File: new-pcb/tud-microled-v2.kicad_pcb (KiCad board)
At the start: 2 copper layers, 100 x 80 mm, 153 parts

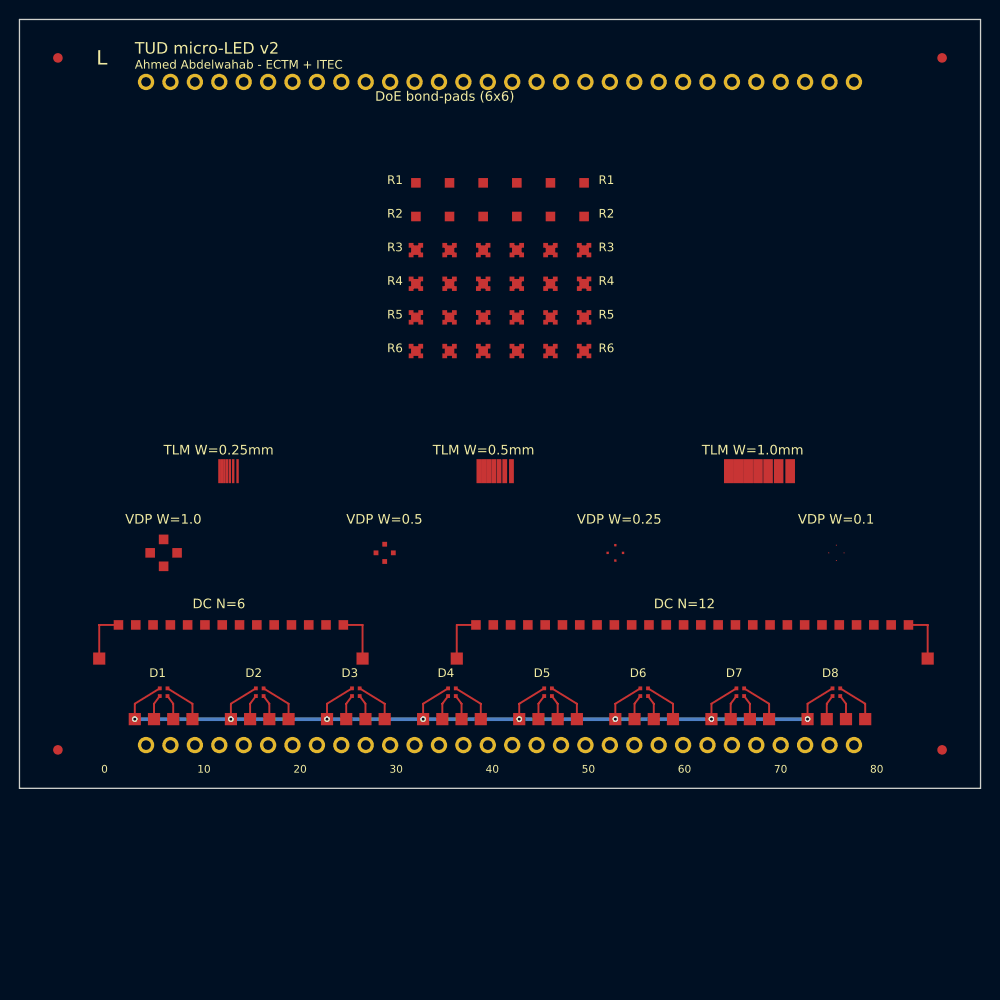
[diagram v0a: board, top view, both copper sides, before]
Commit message: Refactor PCB design settings and update electrical test configuration
- Added a new user-edited backup file for the PCB design with comprehensive settings for design defaults, rules, and dimensions.
- Updated the electrical test configuration by modifying the column widths to ensure proper alignment and sorting in the report.
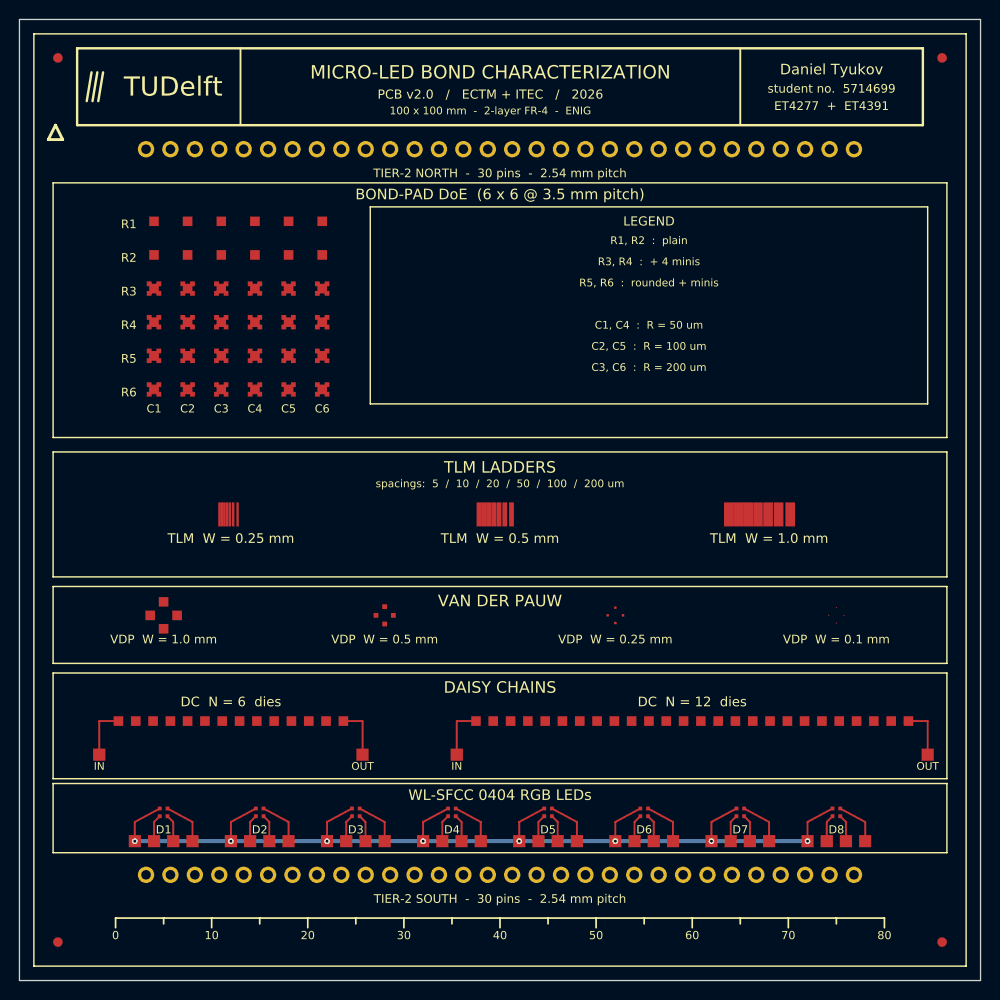
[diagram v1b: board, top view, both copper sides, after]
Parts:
- moved BP_R1C1 27.5 mm to (14.0, 21.0)
- moved BP_R1C2 27.5 mm to (17.5, 21.0)
- moved BP_R1C3 27.5 mm to (21.0, 21.0)
- moved BP_R1C4 27.5 mm to (24.5, 21.0)
- moved BP_R1C5 27.5 mm to (28.0, 21.0)
- moved BP_R1C6 27.5 mm to (31.5, 21.0)
- moved BP_R2C1 27.5 mm to (14.0, 24.5)
- moved BP_R2C2 27.5 mm to (17.5, 24.5)
- moved BP_R2C3 27.5 mm to (21.0, 24.5)
- moved BP_R2C4 27.5 mm to (24.5, 24.5)
- moved BP_R2C5 27.5 mm to (28.0, 24.5)
- moved BP_R2C6 27.5 mm to (31.5, 24.5)
- moved BP_R3C1 27.5 mm to (14.0, 28.0)
- moved BP_R3C2 27.5 mm to (17.5, 28.0)
- moved BP_R3C3 27.5 mm to (21.0, 28.0)
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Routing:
- net LED_VCC: track 107.2 -> 109.6 mm
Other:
- board size 100 x 80 mm -> 100 x 100 mm
- board text added: "100 x 100 mm - 2-layer FR-4 - ENIG"
- board text added: "2-layer FR-4 1.6 mm 1 oz Cu"
- board text added: "ASSEMBLY"
- board text added: "BOND-PAD DoE (6 x 6 @ 3.5 mm pitch)"
- board text added: "BOTTOM - tud-microled-v2 - 2026"
- board text added: "Bonder: Tresky T-3000-PRO"
- board text added: "C1"
- board text added: "C1, C4 : R = 50 um"
- board text added: "C2"
- board text added: "C2, C5 : R = 100 um"
- board text added: "C3"
- board text added: "C3, C6 : R = 200 um"
- board text added: "C4"
- board text added: "C5"
- board text added: "C6"
- board text added: "D1..D8 + PP-* - LEDs and probes"
- board text added: "DAISY CHAINS"
- board text added: "DC - daisy chain (N joints)"
- board text added: "DC N = 12 dies"
- board text added: "DC N = 6 dies"
- board text added: "DESIGNER"
- board text added: "Daniel Tyukov"
- board text added: "Daniel Tyukov - student no. 5714699"
- board text added: "DoE - 6 x 6 isolated bond pads"
- board text added: "ET4277 + ET4391"
- board text added: "ET4277 + ET4391 - TU Delft MSc EE"
- board text added: "FABRICATION"
- board text added: "Finish: ENIG (Ni 4 um / Au 0.075 um)"
- board text added: "IN"
- board text added: "LEGEND"
- board text added: "MICRO-LED BOND CHARACTERIZATION"
- board text added: "Mask: matte green / silk: white"
- board text added: "Metrology: Keyence VK-X250 + X-ray + shear"
- board text added: "Min clearance 0.15 mm / min trace 0.20 mm"
- board text added: "Min via / drill 0.45 / 0.20 mm"
- board text added: "OUT"
- board text added: "PCB v2.0 / ECTM + ITEC / 2026"
- board text added: "Paste: TS391LT Sn42 Bi57.6 Ag0.4"
- board text added: "R1, R2 : plain"
- board text added: "R3, R4 : + 4 minis"
- board text added: "R5, R6 : rounded + minis"
- board text added: "Reflow: hot-plate, peak 165 C"
- board text added: "SECTION KEY"
- board text added: "Stencil: 100 um SS (eC-stencil-mate)"
- board text added: "TIER-2 NORTH - 30 pins - 2.54 mm pitch"
- board text added: "TIER-2 SOUTH - 30 pins - 2.54 mm pitch"
- board text added: "TLM - contact-resistivity ladder"
- board text added: "TLM LADDERS"
- board text added: "TLM W = 0.25 mm"
- board text added: "TLM W = 0.5 mm"
- board text added: "TLM W = 1.0 mm"
- board text added: "TUDelft"
- board text added: "VAN DER PAUW"
- board text added: "VDP - Van der Pauw cloverleaf"
- board text added: "VDP W = 0.1 mm"
- board text added: "VDP W = 0.25 mm"
- board text added: "VDP W = 0.5 mm"
- board text added: "VDP W = 1.0 mm"
- board text added: "WL-SFCC 0404 RGB LEDs"
- board text added: "based on Abdelwahab et al. ECTC 2025"
- board text added: "spacings: 5 / 10 / 20 / 50 / 100 / 200 um"
- board text added: "student no. 5714699"
- board text removed: "Ahmed Abdelwahab - ECTM + ITEC"
- board text removed: "DC N=12"
- board text removed: "DC N=6"
- board text removed: "DoE bond-pads (6x6)"
- board text removed: "L"
- board text removed: "TLM W=0.25mm"
- board text removed: "TLM W=0.5mm"
- board text removed: "TLM W=1.0mm"
- board text removed: "TUD micro-LED v2"
- board text removed: "VDP W=0.1"
- board text removed: "VDP W=0.25"
- board text removed: "VDP W=0.5"
- board text removed: "VDP W=1.0"

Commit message: v3 PCB: 100x100mm board, full silkscreen polish, south header pre-wired
Major changes vs prior v2:
- Board grown 100x80 -> 100x100 mm (room for proper silkscreen)
- Title block redesigned with 3 zones (TUDelft mark / project / student info)
- Section frames around DoE, TLM, VDP, DC, LED rows
- DoE LEGEND box on right with row/column descriptions
- mm ruler at the bottom
- Back-side silkscreen: FABRICATION, ASSEMBLY, DESIGNER, TIER-2 SOUTH PINOUT
- Daniel Tyukov / student no. 5714699 / ET4277 + ET4391 in title + back
- TUDelft mark (stylized flame + wordmark) on both sides
- South header extended to 32 pins, covers ALL 8 LEDs (D1-D8 x A/KG/KB/KR)
- South pre-wired via short F.Cu Manhattan routes (4 lanes by role)
- LED common anode bussed on B.Cu via vias at each LED's A probe
- North header (30 pins) left user-jumperable; pin pads carry assigned net
  for the user's intended VDP/DC/TLM target (documented on back-silk)
- Pin number labels every 5th (1, 5, 10, 15, 20, 25, 30/32)

DRC: 0 violations, 0 unconnected pads, 0 footprint errors.
Iterated 27 times with visual + DRC feedback (see V2_DESIGN_NOTES.md).

Fab outputs regenerated in new-pcb/fab/:
- gerbers/ (zipped)
- STEP 3D, top + bottom PDFs
- position CSV, BOM CSV
- 1800x1800 top + bottom PNG renders
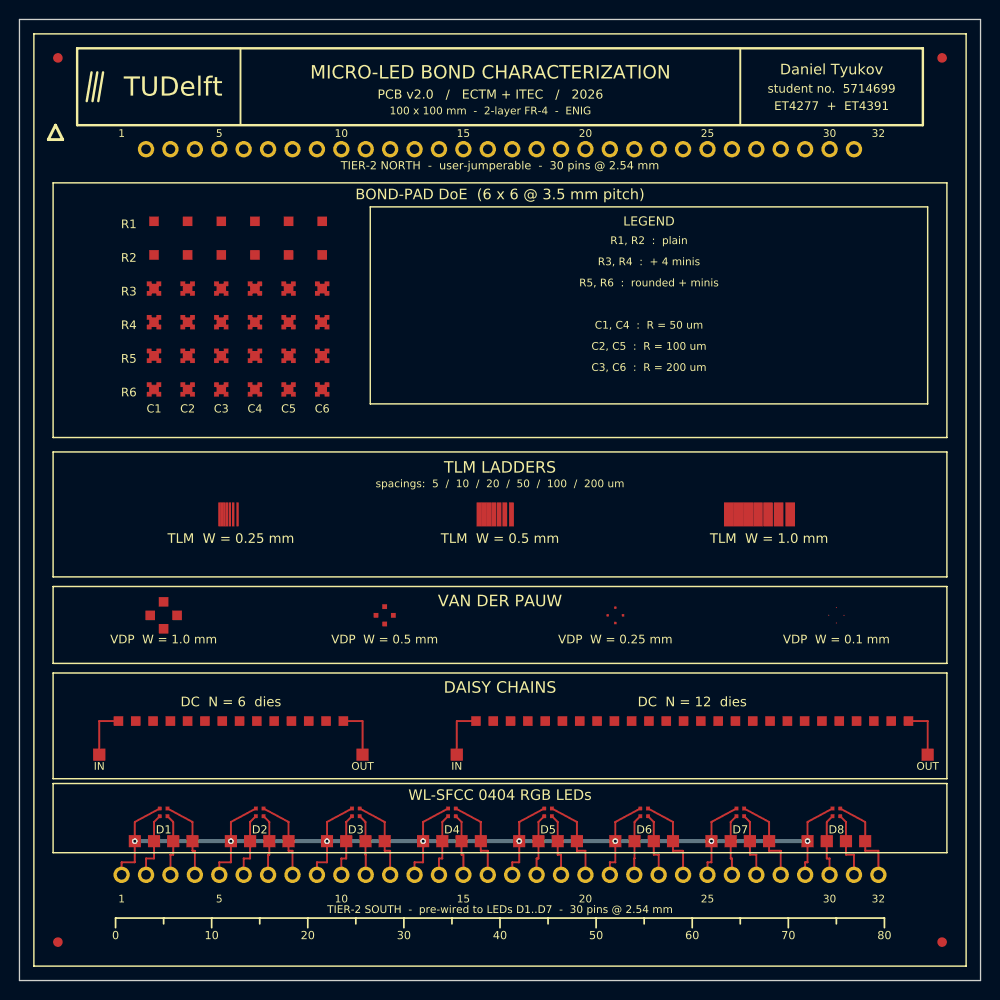
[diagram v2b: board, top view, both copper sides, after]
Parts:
- added H_S_31: H_S_31, Header_2.54mm, F.Cu at (86.8, 89.0)
- added H_S_32: H_S_32, Header_2.54mm, F.Cu at (89.4, 89.0)
- moved H_S_16 2.54 mm to (48.7, 89.0)
- moved H_S_22 2.54 mm to (64.0, 89.0)
- moved H_S_24 2.54 mm to (69.0, 89.0)
- moved H_S_26 2.54 mm to (74.1, 89.0)
- moved H_S_28 2.54 mm to (79.2, 89.0)
- moved H_S_29 2.54 mm to (81.8, 89.0)
- moved H_S_6 2.54 mm to (23.3, 89.0)
- moved H_S_9 2.54 mm to (30.9, 89.0)
- moved H_S_2 2.54 mm to (13.2, 89.0)
- moved H_S_1 2.54 mm to (10.6, 89.0)
- moved H_S_10 2.54 mm to (33.5, 89.0)
- moved H_S_11 2.54 mm to (36.0, 89.0)
- moved H_S_12 2.54 mm to (38.6, 89.0)
- moved H_S_13 2.54 mm to (41.1, 89.0)
- moved H_S_14 2.54 mm to (43.6, 89.0)
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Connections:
- H_S_1 pad 1: (no net) -> LED_VCC
- H_S_10 pad 1: (no net) -> LED3_KG
- H_S_11 pad 1: (no net) -> LED3_KB
- H_S_12 pad 1: (no net) -> LED3_KR
- H_S_13 pad 1: (no net) -> LED_VCC
- H_S_14 pad 1: (no net) -> LED4_KG
- H_S_15 pad 1: (no net) -> LED4_KB
- H_S_16 pad 1: (no net) -> LED4_KR
- H_S_17 pad 1: (no net) -> LED_VCC
- H_S_18 pad 1: (no net) -> LED5_KG
- H_S_19 pad 1: (no net) -> LED5_KB
- H_S_2 pad 1: (no net) -> LED1_KG
- H_S_20 pad 1: (no net) -> LED5_KR
- H_S_21 pad 1: (no net) -> LED_VCC
- H_S_22 pad 1: (no net) -> LED6_KG
- H_S_23 pad 1: (no net) -> LED6_KB
- H_S_24 pad 1: (no net) -> LED6_KR
- H_S_25 pad 1: (no net) -> LED_VCC
- H_S_26 pad 1: (no net) -> LED7_KG
- H_S_27 pad 1: (no net) -> LED7_KB
- H_S_28 pad 1: (no net) -> LED7_KR
- H_S_29 pad 1: (no net) -> LED_VCC
- H_S_3 pad 1: (no net) -> LED1_KB
- H_S_30 pad 1: (no net) -> LED8_KG
- H_S_4 pad 1: (no net) -> LED1_KR
- H_S_5 pad 1: (no net) -> LED_VCC
- H_S_6 pad 1: (no net) -> LED2_KG
- H_S_7 pad 1: (no net) -> LED2_KB
- H_S_8 pad 1: (no net) -> LED2_KR
- H_S_9 pad 1: (no net) -> LED_VCC
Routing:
- net LED_VCC: track 109.6 -> 144.1 mm
- net LED8_KR: track 4.95 -> 9.82 mm
- net LED7_KR: track 4.95 -> 9.66 mm
- net LED6_KR: track 4.95 -> 9.50 mm
- net LED5_KR: track 4.95 -> 9.34 mm
- net LED1_KG: track 2.85 -> 7.18 mm
- net LED8_KB: track 2.85 -> 7.18 mm
- net LED4_KR: track 4.95 -> 9.18 mm
- net LED7_KB: track 2.85 -> 7.02 mm
- net LED2_KG: track 2.85 -> 7.02 mm
- net LED3_KR: track 4.95 -> 9.02 mm
- net LED6_KB: track 2.85 -> 6.86 mm
- net LED3_KG: track 2.85 -> 6.86 mm
- net LED2_KR: track 4.95 -> 8.86 mm
- net LED5_KB: track 2.85 -> 6.70 mm
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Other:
- board text added: "1"
- board text added: "1-4 D1 5-8 D2 9-12 D3 13-16 D4"
- board text added: "15"
- board text added: "17-20 D5 21-24 D6 25-28 D7 29-32 D8"
- board text added: "25"
- board text added: "32"
- board text added: "5"
- board text added: "NORTH row: user-jumperable"
- board text added: "TIER-2 NORTH - user-jumperable - 30 pins @ 2.54 mm"
- board text added: "TIER-2 SOUTH - pre-wired to LEDs D1..D7 - 30 pins @ 2.54 mm"
- board text added: "TIER-2 SOUTH PINOUT"
- board text added: "each group: A, KG, KB, KR (A = LED_VCC)"
- board text removed: "D1..D8 + PP-* - LEDs and probes"
- board text removed: "DC - daisy chain (N joints)"
- board text removed: "DoE - 6 x 6 isolated bond pads"
- board text removed: "SECTION KEY"
- board text removed: "TIER-2 NORTH - 30 pins - 2.54 mm pitch"
- board text removed: "TIER-2 SOUTH - 30 pins - 2.54 mm pitch"
- board text removed: "TLM - contact-resistivity ladder"
- board text removed: "VDP - Van der Pauw cloverleaf"

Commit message: v3.5: add hardware for advanced LED electrical characterization
NEW HARDWARE ADDITIONS (LED-characterization focused):
- 4 x 0402 NTC thermistors (TH1-TH4) between LED pairs for V_F-TSP and
  aging temperature monitoring (Murata NCP15XH103 or compatible)
- 4 x GND probe pads at corners with vias to B.Cu GND pour
- 4 x 1mm gold TC pads (TC1-TC4) at TLM/VDP section edges for soldering
  fine-wire thermocouples during reflow profile measurement
- B.Cu GND pour covering full board (low-impedance return for pulsed-IV
  and AC impedance / EIS measurements)
- Widened LED_VCC bus from 0.4 to 0.8mm (lower inductance pulsed-IV return)
- Silk callout: 'ENIG (all pads gold)' — clarifies all touch points are gold

ENABLES these electrical characterizations on bonded LEDs:
- V_F as junction thermometer (TSP) using NTC for ambient calibration
- AC impedance / EIS via 4-wire access + clean ground return
- Pulsed-IV (low-inductance return path)
- Aging / lifetime stress with temp monitoring
- Real-time reflow profile measurement at bond formation
Plus everything from v3.0 (basic V_F, I-V curve, ideality factor, reverse
leakage) which needed no new hardware.

DRC: 0 errors, 0 unconnected, 1 cosmetic silk warning at frame corner.
Iterated 32 times with visual + DRC feedback to keep silkscreen clean.

Fab outputs regenerated: gerbers/, STEP, top+bottom PDFs, position CSV,
updated BOM (now includes NTCs, TCs, GND pads).
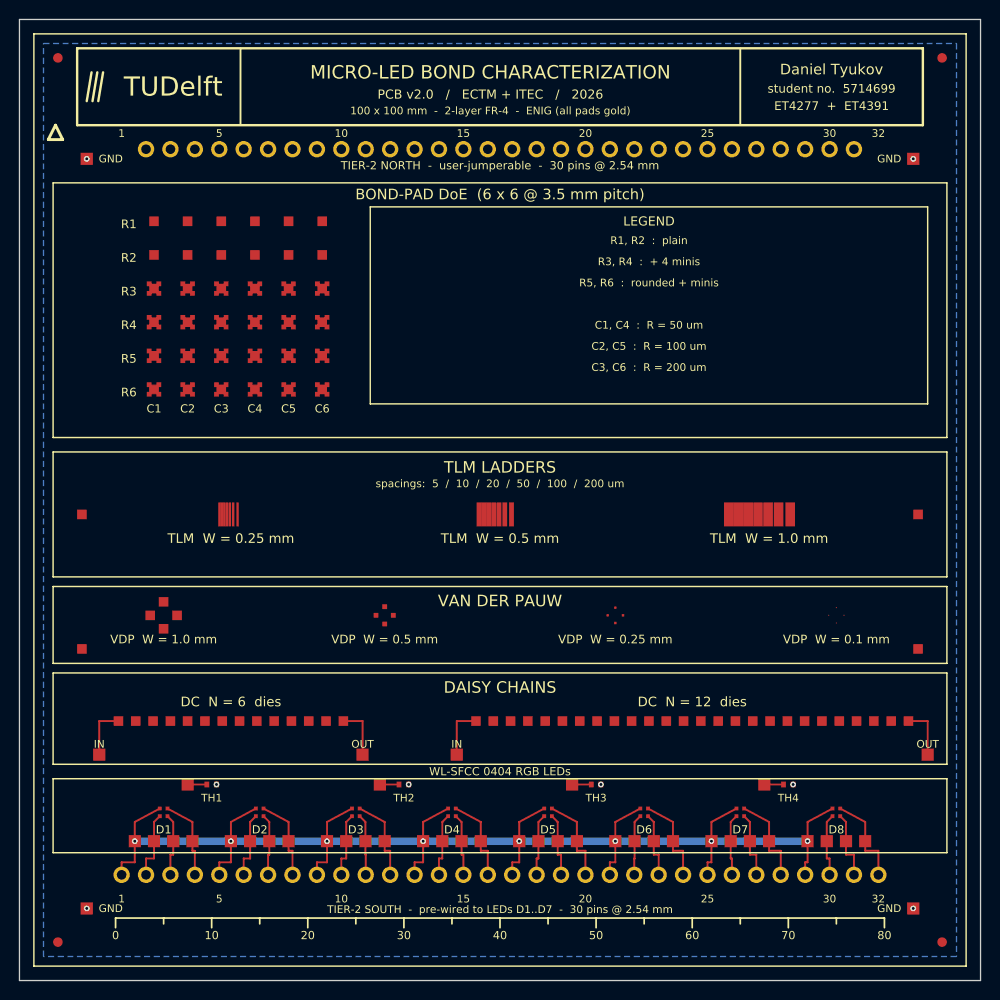
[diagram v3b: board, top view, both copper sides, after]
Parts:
- added PP_GND1: PP_GND1, Probe_1.27mm, F.Cu at (7.00, 14.5)
- added PP_GND2: PP_GND2, Probe_1.27mm, F.Cu at (93.0, 14.5)
- added PP_GND3: PP_GND3, Probe_1.27mm, F.Cu at (7.00, 92.5)
- added PP_GND4: PP_GND4, Probe_1.27mm, F.Cu at (93.0, 92.5)
- added PP_NTC1: PP_NTC1, Probe_1.27mm, F.Cu at (17.5, 79.6)
- added PP_NTC2: PP_NTC2, Probe_1.27mm, F.Cu at (37.5, 79.6)
- added PP_NTC3: PP_NTC3, Probe_1.27mm, F.Cu at (57.5, 79.6)
- added PP_NTC4: PP_NTC4, Probe_1.27mm, F.Cu at (77.5, 79.6)
- added TC1: TC1, TC_Pad_1mm, F.Cu at (6.50, 51.5)
- added TC2: TC2, TC_Pad_1mm, F.Cu at (6.50, 65.5)
- added TC3: TC3, TC_Pad_1mm, F.Cu at (93.5, 51.5)
- added TC4: TC4, TC_Pad_1mm, F.Cu at (93.5, 65.5)
- added TH1: TH1, NTC_0402, F.Cu at (20.0, 79.6)
- added TH2: TH2, NTC_0402, F.Cu at (40.0, 79.6)
- added TH3: TH3, NTC_0402, F.Cu at (60.0, 79.6)
- added TH4: TH4, NTC_0402, F.Cu at (80.0, 79.6)
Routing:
- net NTC4: track 0.00 -> 2.00 mm
- net NTC3: track 0.00 -> 2.00 mm
- net NTC2: track 0.00 -> 2.00 mm
- net NTC1: track 0.00 -> 2.00 mm
- net GND: vias 0 -> 8
- added copper zone on B.Cu, net GND
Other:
- board text added: "100 x 100 mm - 2-layer FR-4 - ENIG (all pads gold)"
- board text added: "GND"
- board text added: "TH1"
- board text added: "TH2"
- board text added: "TH3"
- board text added: "TH4"
- board text removed: "100 x 100 mm - 2-layer FR-4 - ENIG"

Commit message: Refactor code structure for improved readability and maintainability
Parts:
- removed DC_N12: DC_N12, DaisyChain
- removed DC_N6: DC_N6, DaisyChain
- removed PP_DC12_IN: PP_DC12_IN, Probe_1.27mm
- removed PP_DC12_OUT: PP_DC12_OUT, Probe_1.27mm
- removed PP_DC6_IN: PP_DC6_IN, Probe_1.27mm
- removed PP_DC6_OUT: PP_DC6_OUT, Probe_1.27mm
- added DCL12_L1: DCL12_L1, WL-SFCC_0404, F.Cu at (56.2, 73.0)
- added DCL12_L10: DCL12_L10, WL-SFCC_0404, F.Cu at (78.8, 73.0)
- added DCL12_L11: DCL12_L11, WL-SFCC_0404, F.Cu at (81.2, 73.0)
- added DCL12_L12: DCL12_L12, WL-SFCC_0404, F.Cu at (83.8, 73.0)
- added DCL12_L2: DCL12_L2, WL-SFCC_0404, F.Cu at (58.8, 73.0)
- added DCL12_L3: DCL12_L3, WL-SFCC_0404, F.Cu at (61.2, 73.0)
- added DCL12_L4: DCL12_L4, WL-SFCC_0404, F.Cu at (63.8, 73.0)
- added DCL12_L5: DCL12_L5, WL-SFCC_0404, F.Cu at (66.2, 73.0)
- added DCL12_L6: DCL12_L6, WL-SFCC_0404, F.Cu at (68.8, 73.0)
- added DCL12_L7: DCL12_L7, WL-SFCC_0404, F.Cu at (71.2, 73.0)
- added DCL12_L8: DCL12_L8, WL-SFCC_0404, F.Cu at (73.8, 73.0)
- added DCL12_L9: DCL12_L9, WL-SFCC_0404, F.Cu at (76.2, 73.0)
- added DCL6_L1: DCL6_L1, WL-SFCC_0404, F.Cu at (15.8, 73.0)
- added DCL6_L2: DCL6_L2, WL-SFCC_0404, F.Cu at (18.2, 73.0)
- added DCL6_L3: DCL6_L3, WL-SFCC_0404, F.Cu at (20.8, 73.0)
- added DCL6_L4: DCL6_L4, WL-SFCC_0404, F.Cu at (23.2, 73.0)
- added DCL6_L5: DCL6_L5, WL-SFCC_0404, F.Cu at (25.8, 73.0)
- added DCL6_L6: DCL6_L6, WL-SFCC_0404, F.Cu at (28.2, 73.0)
- added PP_DCL12_IN: PP_DCL12_IN, Probe_1.27mm, F.Cu at (53.9, 76.5)
- added PP_DCL12_OUT: PP_DCL12_OUT, Probe_1.27mm, F.Cu at (86.2, 76.5)
- added PP_DCL6_IN: PP_DCL6_IN, Probe_1.27mm, F.Cu at (13.3, 76.5)
- added PP_DCL6_OUT: PP_DCL6_OUT, Probe_1.27mm, F.Cu at (30.6, 76.5)
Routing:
- net DCL6_OUT: track 0.00 -> 5.90 mm
- net DCL6_IN: track 0.00 -> 5.90 mm
- net DCL12_OUT: track 0.00 -> 5.90 mm
- net DCL12_IN: track 0.00 -> 5.90 mm
- net DC_N6_OUT: track 5.50 -> 0.00 mm
- net DC_N6_IN: track 5.50 -> 0.00 mm
- net DC_N12_OUT: track 5.50 -> 0.00 mm
- net DC_N12_IN: track 5.50 -> 0.00 mm
- net DCL6_J5: track 0.00 -> 1.70 mm
- net DCL6_J4: track 0.00 -> 1.70 mm
- net DCL6_J3: track 0.00 -> 1.70 mm
- net DCL6_J2: track 0.00 -> 1.70 mm
- net DCL6_J1: track 0.00 -> 1.70 mm
- net DCL12_J3: track 0.00 -> 1.70 mm
- net DCL12_J2: track 0.00 -> 1.70 mm
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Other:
- board text added: "DC-R N = 12 LEDs"
- board text added: "DC-R N = 6 LEDs"
- board text added: "LED DAISY CHAINS"
- board text removed: "DAISY CHAINS"
- board text removed: "DC N = 12 dies"
- board text removed: "DC N = 6 dies"
